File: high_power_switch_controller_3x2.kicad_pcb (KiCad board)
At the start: 2 copper layers, 69.8 x 40.6 mm, 1 part

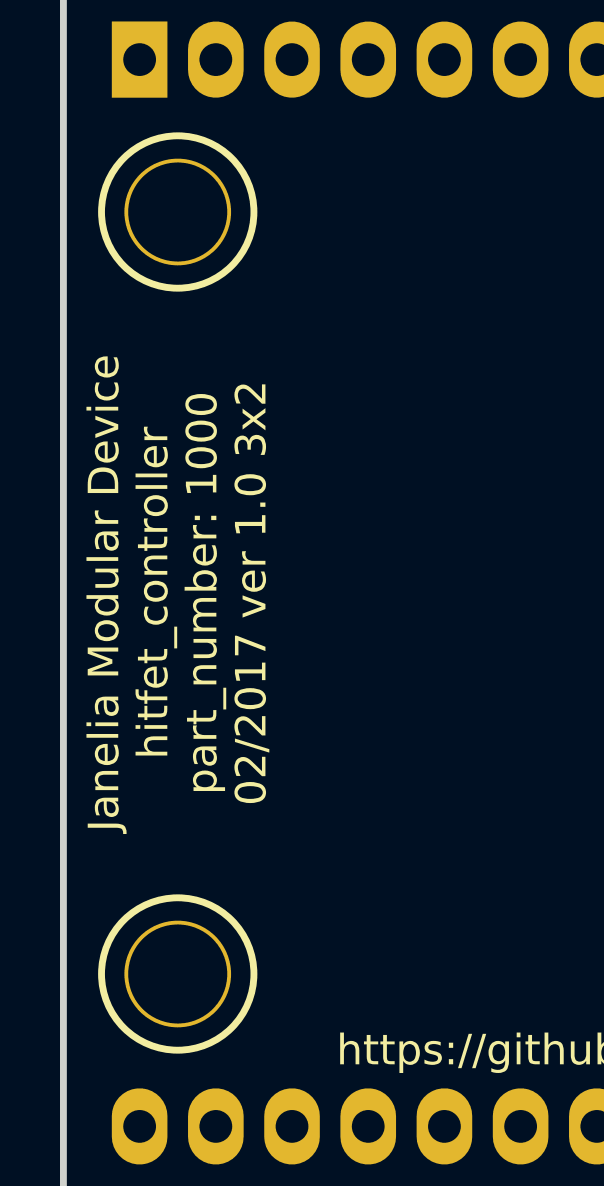
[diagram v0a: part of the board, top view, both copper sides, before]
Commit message: hitfet -> high_power_switch.
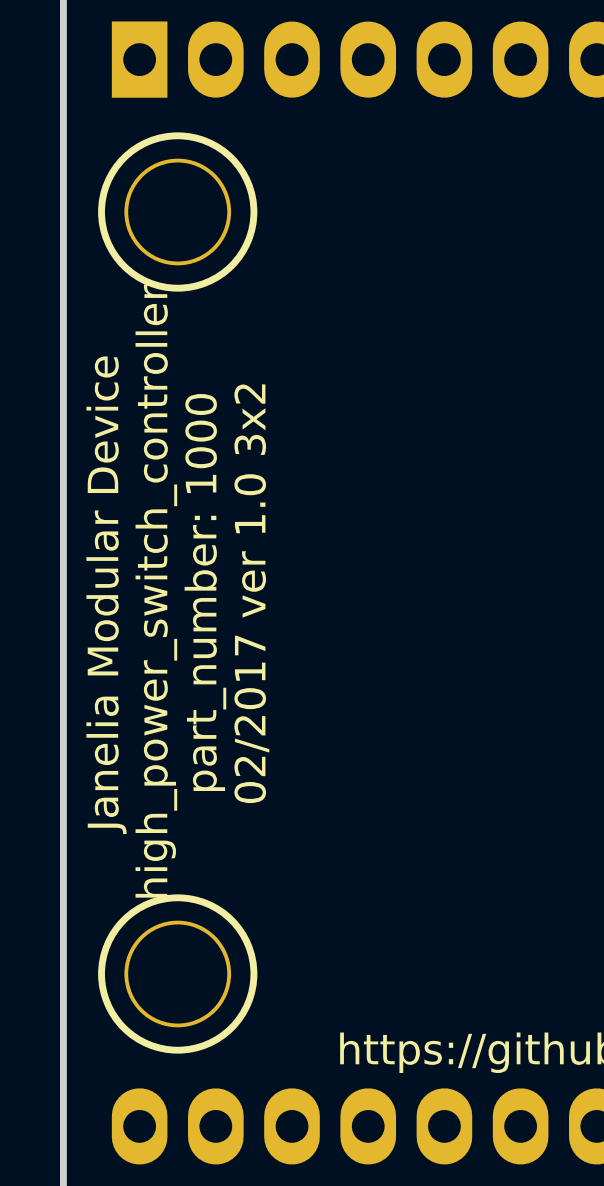
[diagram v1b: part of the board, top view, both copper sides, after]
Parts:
- MDB1: footprint hitfet_controller_3x2:MODULAR_DEVICE_BASE_3X2_MALE -> high_power_switch_controller_3x2:MODULAR_DEVICE_BASE_3X2_MALE
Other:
- board text added: "Janelia Modular Device high_power_switch_controller part_number: 1000 02/2017 ver 1.0 3x2"
- board text removed: "Janelia Modular Device hitfet_controller part_number: 1000 02/2017 ver 1.0 3x2"
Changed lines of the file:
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@@
   (page A4)
   (title_block
-    (title hitfet_controller_3x2)
+    (title high_power_switch_controller_3x2)
     (rev 1.0)
   )
@@
     (diff_pair_width 0.254)
   )
-  (module hitfet_controller_3x2:MODULAR_DEVICE_BASE_3X2_MALE (layer F.Cu)
+  (module high_power_switch_controller_3x2:MODULAR_DEVICE_BASE_3X2_MALE (layer F.Cu)
     (at 107.315 88.9)
     (fp_text reference MDB1 (at 0 0) (layer F.SilkS) hide
@@
     (effects (font (size 1.016 1.016) (thickness 0.1905)))
   )
-  (gr_text "Janelia Modular Device\nhitfet_controller\npart_number: 1000\n02/2017 ver 1.0 3x2" (at 89.535 88.9 90) (layer F.SilkS)
+  (gr_text "Janelia Modular Device\nhigh_power_switch_controller\npart_number: 1000\n02/2017 ver 1.0 3x2" (at 89.535 88.9 90) (layer F.SilkS)
     (effects (font (size 1.016 1.016) (thickness 0.254)))
   )
